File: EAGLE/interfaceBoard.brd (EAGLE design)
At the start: 76.2 x 22.5 mm, 7 parts, among them SW1 EC12E_SW

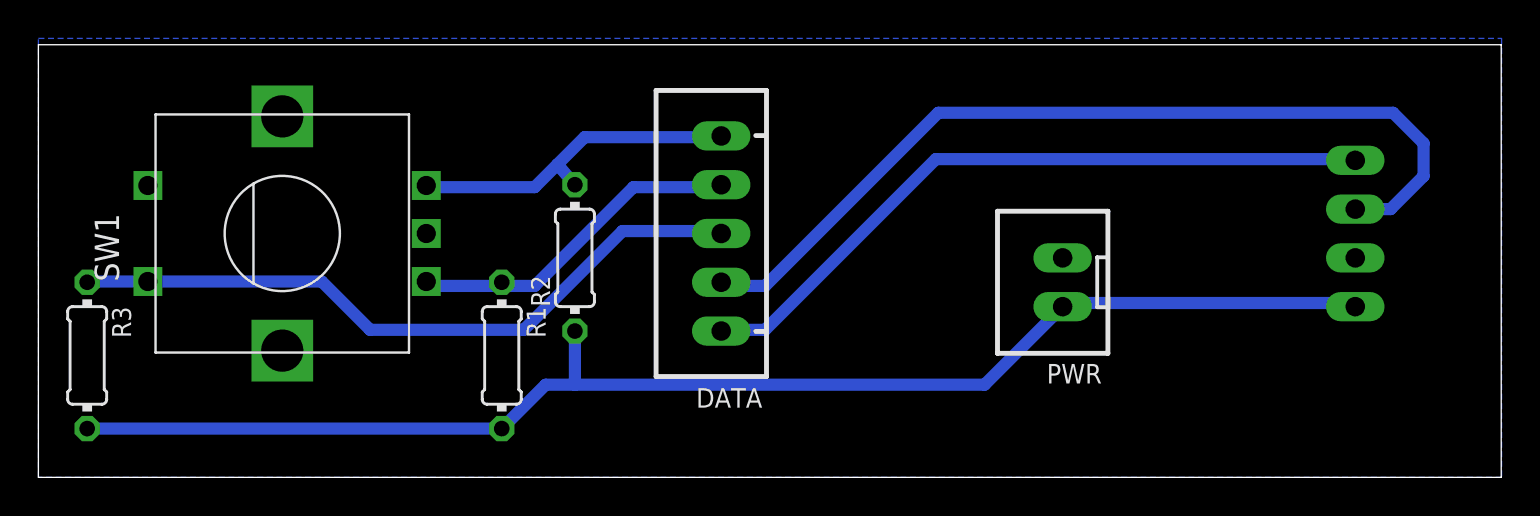
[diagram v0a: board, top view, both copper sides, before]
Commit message: * Small fix where the +5v and GND rail was reversed to the LCD screen on the interface board
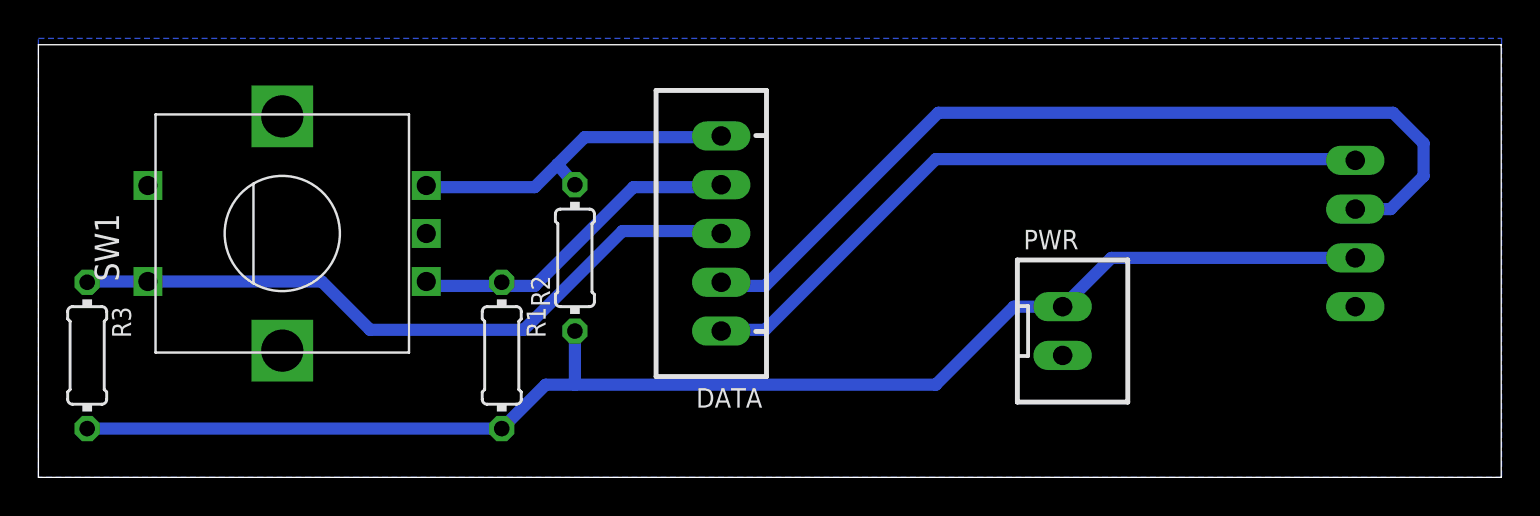
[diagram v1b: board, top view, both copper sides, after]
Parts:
- moved PWR 2.54 mm to (53.3, 7.62), turned to 270 degrees
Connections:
- net +5V: now also SCREEN.2; no longer SCREEN.1
- net GND: now also SCREEN.1; no longer SCREEN.2
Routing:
- net +5V: track 71.6 -> 72.5 mm
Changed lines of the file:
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@@
 <wire x1="76.18" y1="22.53" x2="0" y2="22.53" width="0" layer="20"/>
 <wire x1="0" y1="22.53" x2="0" y2="0" width="0" layer="20"/>
+<dimension x1="0" y1="24.13" x2="76.2" y2="24.13" x3="38.1" y3="29.21" textsize="1.778" layer="1"/>
+<dimension x1="-1.27" y1="22.86" x2="-1.27" y2="0" x3="-6.35" y3="11.43" textsize="1.778" layer="1"/>
 </plain>
 <attributes>
@@
 <attribute name="VALUE" x="21.7" y="16.2" size="1.27" layer="27" rot="R270"/>
 </element>
-<element name="PWR" library="Rembrandt Electronics - JST XH Connectors v1-0" package="JST-XH-02-PACKAGE-LONG-PAD" value="JST-XH-02-PIN-LONG-PAD" x="53.34" y="10.16" smashed="yes" rot="R90">
-<attribute name="NAME" x="55.38" y="5.905" size="1.016" layer="25" ratio="10" rot="R180"/>
-<attribute name="VALUE" x="49.4475" y="6.8575" size="1.016" layer="27" ratio="10" rot="R90"/>
+<element name="PWR" library="Rembrandt Electronics - JST XH Connectors v1-0" package="JST-XH-02-PACKAGE-LONG-PAD" value="JST-XH-02-PIN-LONG-PAD" x="53.34" y="7.62" smashed="yes" rot="R270">
+<attribute name="NAME" x="51.3" y="11.875" size="1.016" layer="25" ratio="10"/>
+<attribute name="VALUE" x="57.2325" y="10.9225" size="1.016" layer="27" ratio="10" rot="R270"/>
 </element>
 <element name="DATA" library="Rembrandt Electronics - JST XH Connectors v1-0" package="JST-XH-05-PACKAGE-LONG-PAD" value="JST-XH-05-PIN-LONG-PAD" x="35.56" y="12.7" smashed="yes" rot="R90">
@@
 <contactref element="SW1" pad="C"/>
 <contactref element="SW1" pad="E"/>
-<contactref element="SCREEN" pad="2"/>
 <polygon width="0.1524" layer="16">
 <vertex x="0" y="22.86"/>
@@
 <vertex x="0" y="0"/>
 </polygon>
+<contactref element="SCREEN" pad="1"/>
 </signal>
 <signal name="+5V">
@@
 <contactref element="R2" pad="1"/>
 <contactref element="R3" pad="2"/>
-<contactref element="SCREEN" pad="1"/>
-<wire x1="68.58" y1="8.89" x2="68.3895" y2="9.0805" width="0.635" layer="16"/>
-<wire x1="68.3895" y1="9.0805" x2="53.5305" y2="9.0805" width="0.635" layer="16"/>
-<wire x1="53.34" y1="8.89" x2="53.5305" y2="9.0805" width="0.635" layer="16"/>
 <wire x1="24.13" y1="2.54" x2="2.54" y2="2.54" width="0.635" layer="16"/>
 <wire x1="27.94" y1="7.62" x2="27.94" y2="4.826" width="0.635" layer="16"/>
-<wire x1="49.276" y1="4.826" x2="53.34" y2="8.89" width="0.635" layer="16"/>
-<wire x1="27.94" y1="4.826" x2="49.276" y2="4.826" width="0.635" layer="16"/>
+<wire x1="50.8" y1="8.89" x2="53.34" y2="8.89" width="0.635" layer="16"/>
+<wire x1="50.8" y1="8.89" x2="46.736" y2="4.826" width="0.635" layer="16"/>
+<wire x1="27.94" y1="4.826" x2="46.736" y2="4.826" width="0.635" layer="16"/>
 <wire x1="24.13" y1="2.54" x2="26.416" y2="4.826" width="0.635" layer="16"/>
 <wire x1="26.416" y1="4.826" x2="27.94" y2="4.826" width="0.635" layer="16"/>
+<contactref element="SCREEN" pad="2"/>
+<wire x1="53.34" y1="8.89" x2="55.88" y2="11.43" width="0.635" layer="16"/>
+<wire x1="55.88" y1="11.43" x2="68.58" y2="11.43" width="0.635" layer="16"/>
 </signal>
 <signal name="CLK">
